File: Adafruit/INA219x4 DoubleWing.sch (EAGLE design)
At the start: 42 parts, among them J1 3.5mm, J2 3.5mm, J3 3.5mm, J4 3.5mm, U1 INA219BIDCNT, U2 INA219BIDCNT, U3 INA219BIDCNT, U4 INA219BIDCNT

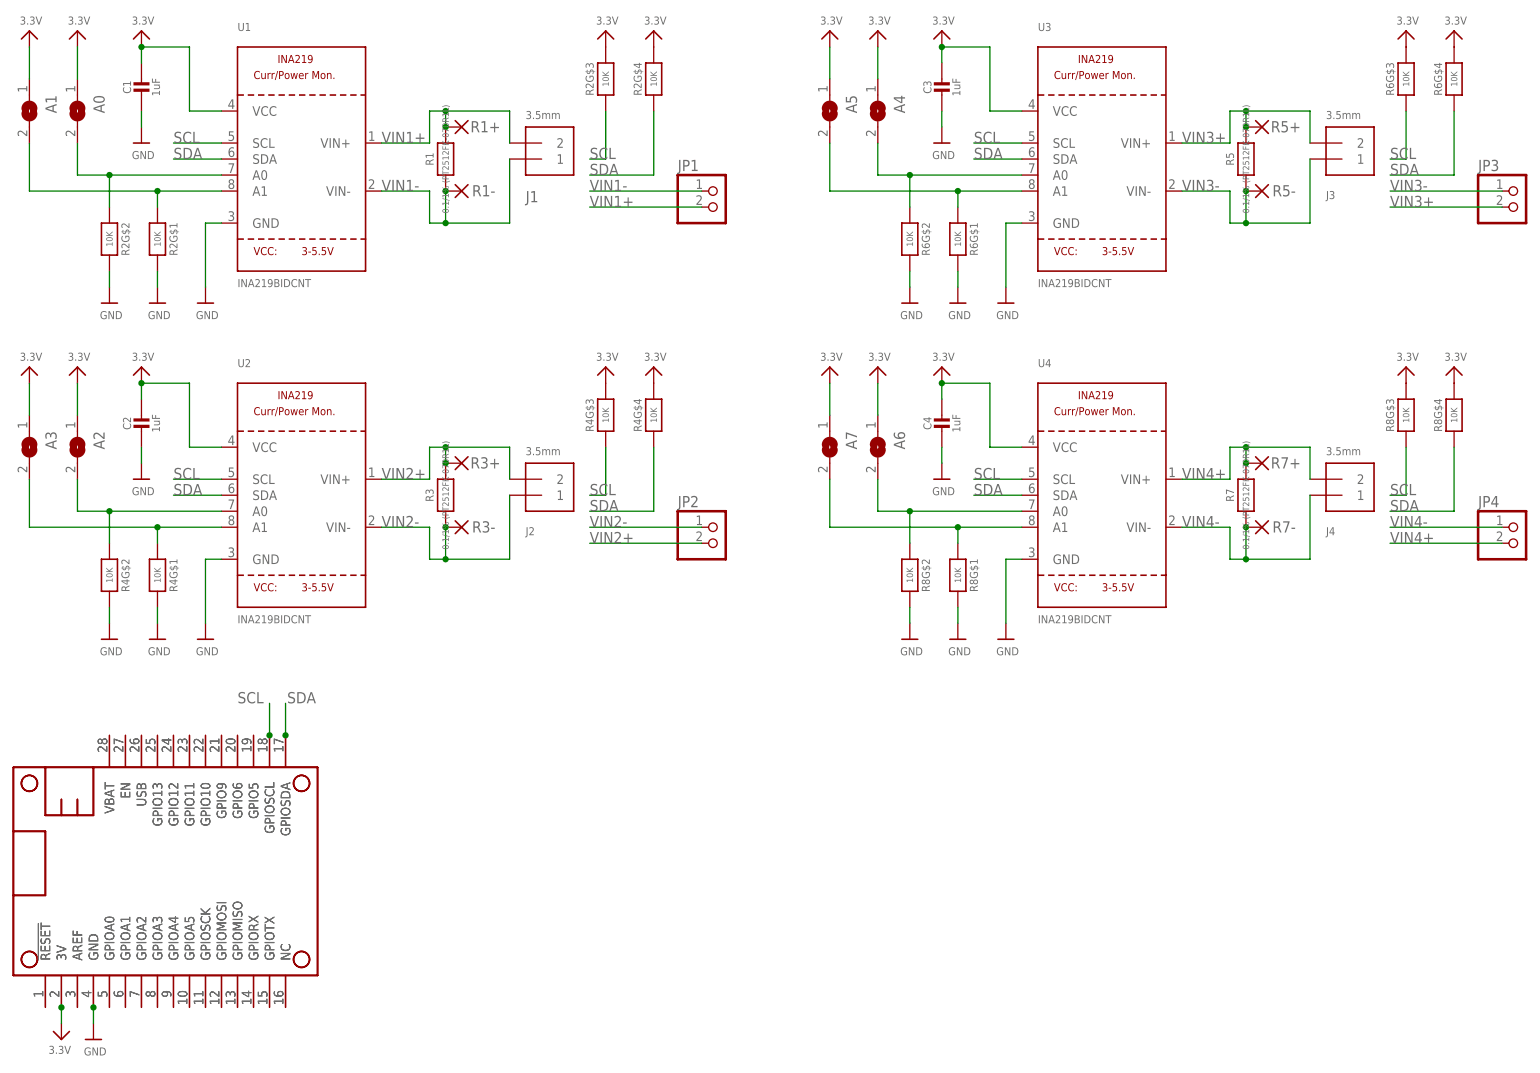
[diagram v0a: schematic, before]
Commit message: Renaming "INA219x4 FeatherWing" to "INA219x4 DoubleWing"
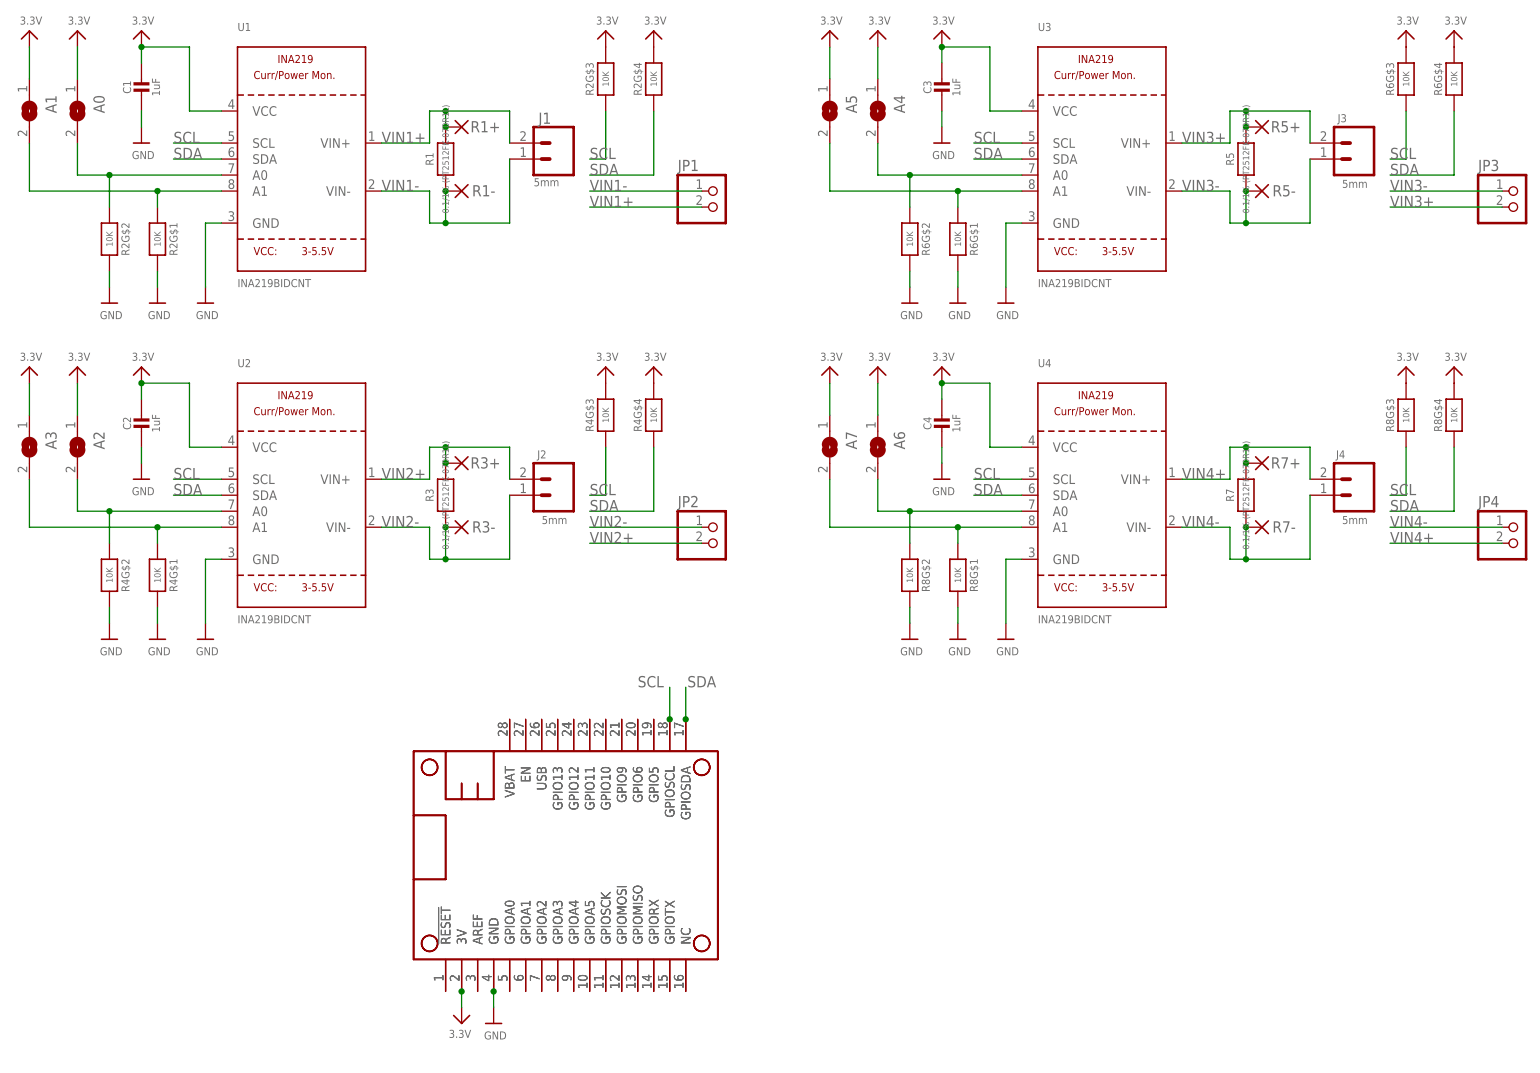
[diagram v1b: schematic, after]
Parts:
- J1, J2, J3, J4: value 3.5mm -> 5mm; device microbuilder:TERMBLOCK_1X2 -> SparkFun-Connectors:CONN_025MM
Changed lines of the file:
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@@
 <layer number="112" name="tSilk" color="7" fill="1" visible="yes" active="yes"/>
 <layer number="113" name="ReferenceLS" color="7" fill="1" visible="no" active="no"/>
+<layer number="114" name="Badge_Outline" color="7" fill="1" visible="yes" active="yes"/>
+<layer number="115" name="ReferenceISLANDS" color="7" fill="1" visible="yes" active="yes"/>
 <layer number="116" name="Patch_BOT" color="9" fill="4" visible="yes" active="yes"/>
 <layer number="118" name="Rect_Pads" color="7" fill="1" visible="no" active="no"/>
@@
 <part name="U$5" library="microbuilder" deviceset="GND" device=""/>
 <part name="R1" library="microbuilder" deviceset="RESISTOR" device="2512" value="0.1/1% (PT2512FK-070R1L)"/>
-<part name="J1" library="microbuilder" deviceset="TERMBLOCK_1X2" device="" value="3.5mm"/>
+<part name="J1" library="SparkFun-Connectors" library_urn="urn:adsk.eagle:library:513" deviceset="CONN_02" device="5MM" package3d_urn="urn:adsk.eagle:package:38044/1" value="5mm"/>
 <part name="U$7" library="microbuilder" deviceset="3.3V" device=""/>
 <part name="U$8" library="microbuilder" deviceset="3.3V" device=""/>
@@
 <part name="U$21" library="microbuilder" deviceset="GND" device=""/>
 <part name="R3" library="microbuilder" deviceset="RESISTOR" device="2512" value="0.1/1% (PT2512FK-070R1L)"/>
-<part name="J2" library="microbuilder" deviceset="TERMBLOCK_1X2" device="" value="3.5mm"/>
+<part name="J2" library="SparkFun-Connectors" library_urn="urn:adsk.eagle:library:513" deviceset="CONN_02" device="5MM" package3d_urn="urn:adsk.eagle:package:38044/1" value="5mm"/>
 <part name="U$22" library="microbuilder" deviceset="3.3V" device=""/>
 <part name="U$23" library="microbuilder" deviceset="3.3V" device=""/>
@@
 <part name="U$16" library="microbuilder" deviceset="GND" device=""/>
 <part name="R5" library="microbuilder" deviceset="RESISTOR" device="2512" value="0.1/1% (PT2512FK-070R1L)"/>
-<part name="J3" library="microbuilder" deviceset="TERMBLOCK_1X2" device="" value="3.5mm"/>
+<part name="J3" library="SparkFun-Connectors" library_urn="urn:adsk.eagle:library:513" deviceset="CONN_02" device="5MM" package3d_urn="urn:adsk.eagle:package:38044/1" value="5mm"/>
 <part name="U$17" library="microbuilder" deviceset="3.3V" device=""/>
 <part name="U$27" library="microbuilder" deviceset="3.3V" device=""/>
@@
 <part name="U$34" library="microbuilder" deviceset="GND" device=""/>
 <part name="R7" library="microbuilder" deviceset="RESISTOR" device="2512" value="0.1/1% (PT2512FK-070R1L)"/>
-<part name="J4" library="microbuilder" deviceset="TERMBLOCK_1X2" device="" value="3.5mm"/>
+<part name="J4" library="SparkFun-Connectors" library_urn="urn:adsk.eagle:library:513" deviceset="CONN_02" device="5MM" package3d_urn="urn:adsk.eagle:package:38044/1" value="5mm"/>
 <part name="U$35" library="microbuilder" deviceset="3.3V" device=""/>
 <part name="U$36" library="microbuilder" deviceset="3.3V" device=""/>
@@
 <attribute name="SHEET" x="230.505" y="10.16" size="2.54" layer="94" font="vector"/>
 </instance>
-<instance part="MS1" gate="G$1" x="7.62" y="17.78" smashed="yes"/>
-<instance part="MS2" gate="G$1" x="7.62" y="17.78" smashed="yes"/>
+<instance part="MS1" gate="G$1" x="71.12" y="20.32" smashed="yes"/>
+<instance part="MS2" gate="G$1" x="71.12" y="20.32" smashed="yes"/>
 <instance part="U1" gate="G$1" x="53.34" y="147.32" smashed="yes">
 <attribute name="NAME" x="43.18" y="167.64" size="1.27" layer="95"/>
@@
 <attribute name="VALUE" x="76.2" y="147.32" size="1.016" layer="96" font="vector" ratio="15" rot="R90" align="center"/>
 </instance>
-<instance part="J1" gate="G$1" x="91.44" y="149.86" smashed="yes" rot="MR180">
-<attribute name="VALUE" x="88.9" y="154.94" size="1.27" layer="96" rot="MR180"/>
-<attribute name="NAME" x="88.9" y="142.24" size="1.778" layer="95" rot="MR180"/>
+<instance part="J1" gate="G$1" x="93.98" y="147.32" smashed="yes" rot="MR0">
+<attribute name="VALUE" x="94.234" y="143.002" size="1.27" layer="96" rot="MR0"/>
+<attribute name="NAME" x="92.964" y="152.908" size="1.778" layer="95" rot="MR0"/>
 </instance>
 <instance part="U$7" gate="G$1" x="10.16" y="167.64" smashed="yes">
@@
 <attribute name="VALUE" x="76.2" y="93.98" size="1.016" layer="96" font="vector" ratio="15" rot="R90" align="center"/>
 </instance>
-<instance part="J2" gate="G$1" x="91.44" y="96.52" smashed="yes" rot="MR180">
-<attribute name="VALUE" x="88.9" y="101.6" size="1.27" layer="96" rot="MR180"/>
-<attribute name="NAME" x="88.9" y="88.9" size="1.27" layer="95" rot="MR180"/>
+<instance part="J2" gate="G$1" x="93.98" y="93.98" smashed="yes" rot="MR0">
+<attribute name="VALUE" x="95.504" y="89.408" size="1.27" layer="96" rot="MR0"/>
+<attribute name="NAME" x="92.202" y="99.822" size="1.27" layer="95" rot="MR0"/>
 </instance>
 <instance part="U$22" gate="G$1" x="10.16" y="114.3" smashed="yes">
@@
 <attribute name="VALUE" x="79.883" y="145.542" size="1.778" layer="96" rot="R180"/>
 </instance>
-<instance part="U$6" gate="G$1" x="20.32" y="7.62" smashed="yes">
-<attribute name="VALUE" x="18.796" y="5.08" size="1.27" layer="96"/>
-</instance>
-<instance part="U$12" gate="G$1" x="15.24" y="7.62" smashed="yes" rot="R180">
-<attribute name="VALUE" x="16.764" y="6.604" size="1.27" layer="96" rot="R180"/>
+<instance part="U$6" gate="G$1" x="83.82" y="10.16" smashed="yes">
+<attribute name="VALUE" x="82.296" y="7.62" size="1.27" layer="96"/>
+</instance>
+<instance part="U$12" gate="G$1" x="78.74" y="10.16" smashed="yes" rot="R180">
+<attribute name="VALUE" x="80.264" y="9.144" size="1.27" layer="96" rot="R180"/>
 </instance>
 <instance part="U3" gate="G$1" x="180.34" y="147.32" smashed="yes">
@@
 <attribute name="VALUE" x="203.2" y="147.32" size="1.016" layer="96" font="vector" ratio="15" rot="R90" align="center"/>
 </instance>
-<instance part="J3" gate="G$1" x="218.44" y="149.86" smashed="yes" rot="MR180">
-<attribute name="VALUE" x="215.9" y="154.94" size="1.27" layer="96" rot="MR180"/>
-<attribute name="NAME" x="215.9" y="142.24" size="1.27" layer="95" rot="MR180"/>
+<instance part="J3" gate="G$1" x="220.98" y="147.32" smashed="yes" rot="MR0">
+<attribute name="VALUE" x="222.504" y="142.748" size="1.27" layer="96" rot="MR0"/>
+<attribute name="NAME" x="219.202" y="153.162" size="1.27" layer="95" rot="MR0"/>
 </instance>
 <instance part="U$17" gate="G$1" x="137.16" y="167.64" smashed="yes">
@@
 <attribute name="VALUE" x="203.2" y="93.98" size="1.016" layer="96" font="vector" ratio="15" rot="R90" align="center"/>
 </instance>
-<instance part="J4" gate="G$1" x="218.44" y="96.52" smashed="yes" rot="MR180">
-<attribute name="VALUE" x="215.9" y="101.6" size="1.27" layer="96" rot="MR180"/>
-<attribute name="NAME" x="215.9" y="88.9" size="1.27" layer="95" rot="MR180"/>
+<instance part="J4" gate="G$1" x="220.98" y="93.98" smashed="yes" rot="MR0">
+<attribute name="VALUE" x="222.504" y="89.408" size="1.27" layer="96" rot="MR0"/>
+<attribute name="NAME" x="218.948" y="99.822" size="1.27" layer="95" rot="MR0"/>
 </instance>
 <instance part="U$35" gate="G$1" x="137.16" y="114.3" smashed="yes">
@@
 <pinref part="MS2" gate="G$1" pin="GND"/>
 <pinref part="U$6" gate="G$1" pin="GND"/>
-<wire x1="20.32" y1="12.7" x2="20.32" y2="10.16" width="0.1524" layer="91"/>
-<junction x="20.32" y="12.7"/>
+<wire x1="83.82" y1="15.24" x2="83.82" y2="12.7" width="0.1524" layer="91"/>
+<junction x="83.82" y="15.24"/>
 </segment>
 <segment>
@@
 <pinref part="MS1" gate="G$1" pin="GPIOSCL"/>
 <pinref part="MS2" gate="G$1" pin="GPIOSCL"/>
-<wire x1="48.26" y1="55.88" x2="48.26" y2="60.96" width="0.1524" layer="91"/>
-<junction x="48.26" y="55.88"/>
-<label x="43.18" y="60.96" size="1.778" layer="95"/>
+<wire x1="111.76" y1="58.42" x2="111.76" y2="63.5" width="0.1524" layer="91"/>
+<junction x="111.76" y="58.42"/>
+<label x="106.68" y="63.5" size="1.778" layer="95"/>
 </segment>
 <segment>
@@
 <pinref part="MS1" gate="G$1" pin="GPIOSDA"/>
 <pinref part="MS2" gate="G$1" pin="GPIOSDA"/>
-<wire x1="50.8" y1="55.88" x2="50.8" y2="60.96" width="0.1524" layer="91"/>
-<junction x="50.8" y="55.88"/>
-<label x="51.054" y="60.96" size="1.778" layer="95"/>
+<wire x1="114.3" y1="58.42" x2="114.3" y2="63.5" width="0.1524" layer="91"/>
+<junction x="114.3" y="58.42"/>
+<label x="114.554" y="63.5" size="1.778" layer="95"/>
 </segment>
 <segment>
@@
 <pinref part="MS2" gate="G$1" pin="3V"/>
 <pinref part="U$12" gate="G$1" pin="3.3V"/>
-<wire x1="15.24" y1="12.7" x2="15.24" y2="10.16" width="0.1524" layer="91"/>
-<junction x="15.24" y="12.7"/>
-</segment>
-<segment>
+<wire x1="78.74" y1="15.24" x2="78.74" y2="12.7" width="0.1524" layer="91"/>
+<junction x="78.74" y="15.24"/>
+</segment>
+<segment>

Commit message: Updated to version that was sent to oshpark for fabrication
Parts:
- removed JP1, JP2, JP3, JP4: (no value), microbuilder:HEADER-1X2ROUND
- added J5, J7: 5mm, SparkFun-Connectors:CONN_025MM
- added J6, J8: (no value), SparkFun-Connectors:CONN_01
- J2, J4: value 5mm -> (none); device SparkFun-Connectors:CONN_025MM -> SparkFun-Connectors:CONN_01
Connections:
- net GND: now also J2.1, J4.1, J6.1, J8.1
- net VIN1+: no longer JP1.2
- net VIN1-: no longer JP1.1
- net VIN2+: now also J3.2; no longer J2.2, JP2.2
- net VIN2-: now also J3.1; no longer J2.1, JP2.1
- net VIN3+: now also J5.2; no longer J3.2, JP3.2
- net VIN3-: now also J5.1; no longer J3.1, JP3.1
- net VIN4+: now also J7.2; no longer J4.2, JP4.2
- net VIN4-: now also J7.1; no longer J4.1, JP4.1
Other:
- moved on the sheet: J3
